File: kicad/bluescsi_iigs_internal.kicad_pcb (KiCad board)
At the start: 2 copper layers, 61.5 x 55.4 mm, 27 parts, among them J1 Conn_02x13_Odd_Even, J2 Conn_02x13_Odd_Even, J3 105162-0001, J4 Conn_01x02_Male, J5 Conn_01x02_Male, J6 DB25_Male, M1 Screw_Terminal_01x01, M2 Screw_Terminal_01x01, SW1 SW_SPDT, U1 YAAJ_BluePill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

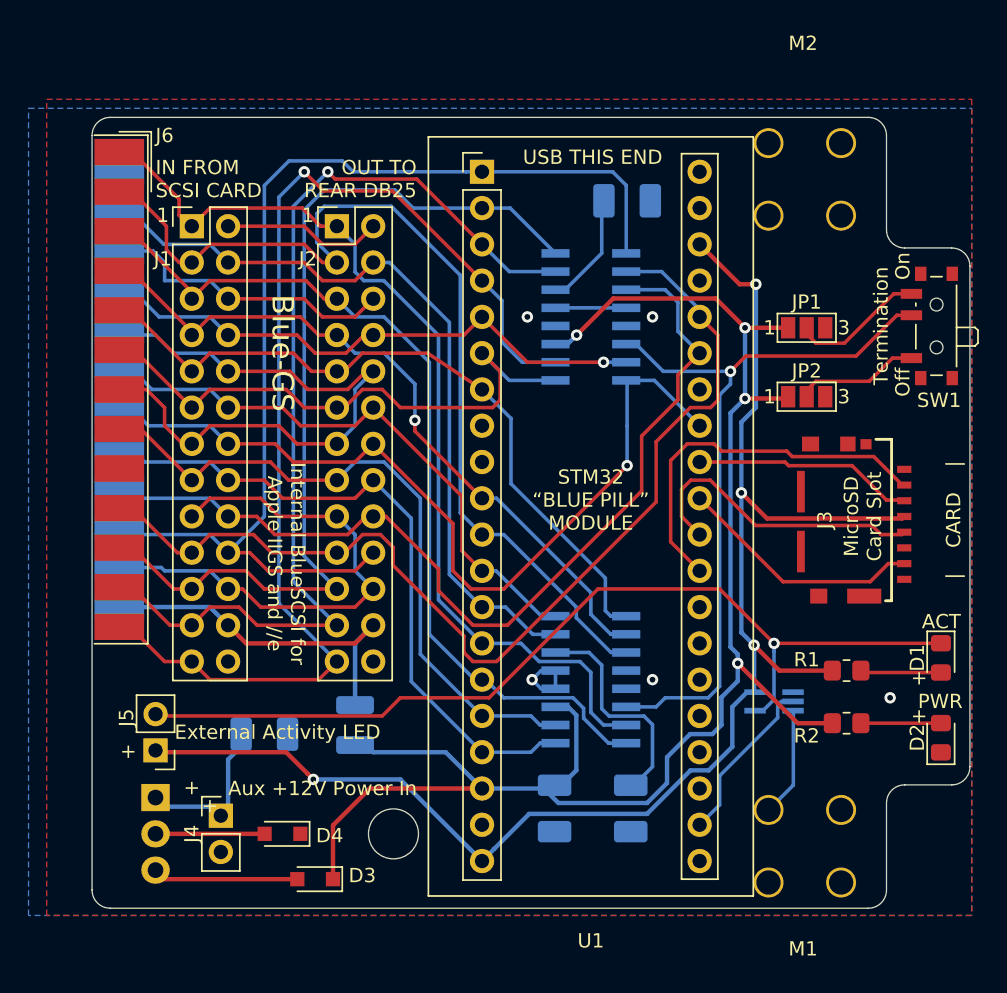
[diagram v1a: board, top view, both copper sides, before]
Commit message: Change silkscreens and legends, reroute 3.3v line for better grounding
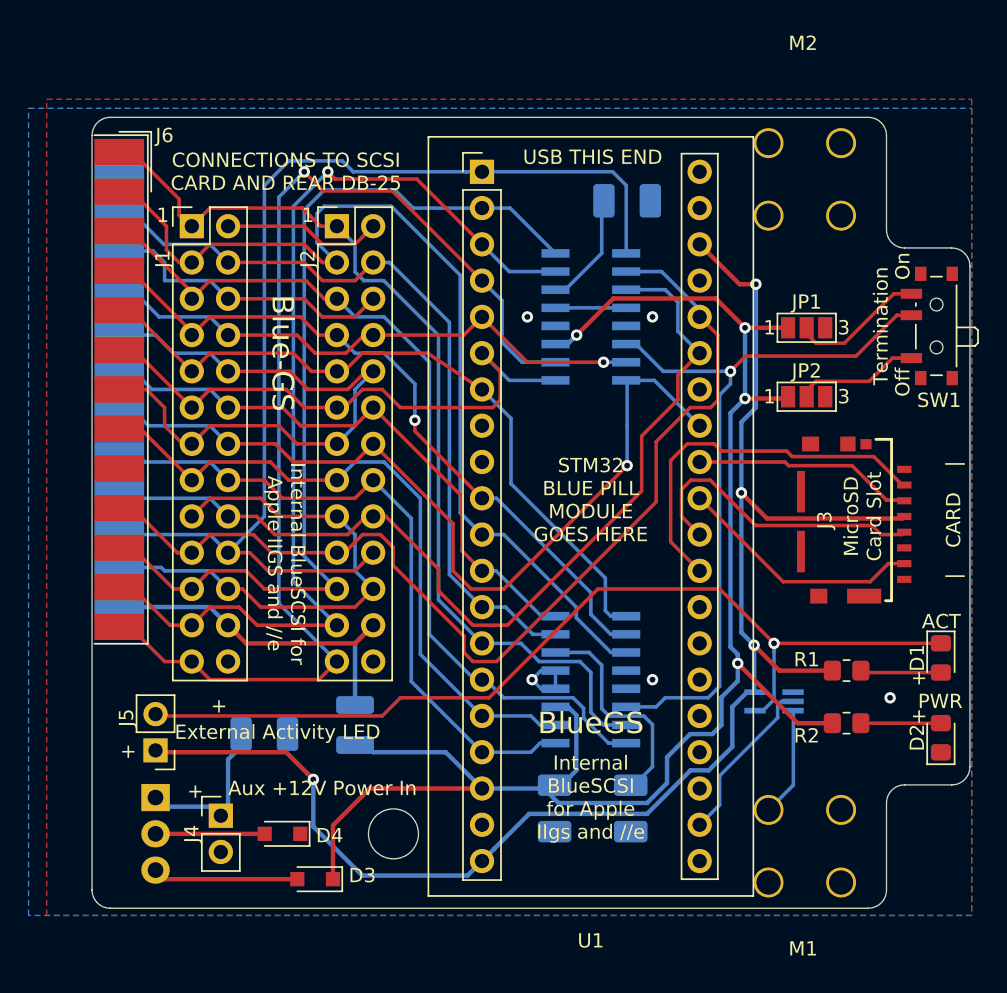
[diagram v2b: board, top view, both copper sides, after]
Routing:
- net +3V3: track 104.0 -> 106.8 mm
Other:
- board text added: "BlueGS"
- board text added: "CONNECTIONS TO SCSI CARD AND REAR DB-25"
- board text added: "Internal BlueSCSI for Apple IIgs and //e"
- board text added: "STM32 BLUE PILL MODULE GOES HERE"
- board text removed: "For Apple Rev. C SCSI and cards with compatible connector"
- board text removed: "IN FROM SCSI CARD"
- board text removed: "OUT TO REAR DB25"
- board text removed: "STM32 “BLUE PILL” MODULE"
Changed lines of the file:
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@@
     (thickness 1.6)
     (drawings 59)
-    (tracks 579)
+    (tracks 581)
     (zones 0)
     (modules 27)
@@
     (descr "Through hole straight pin header, 2x13, 2.54mm pitch, double rows")
     (tags "Through hole pin header THT 2x13 2.54mm double row")
-    (fp_text reference J2 (at -2.032 2.286) (layer F.SilkS)
+    (fp_text reference J2 (at -2.032 2.286 90) (layer F.SilkS)
       (effects (font (size 1 1) (thickness 0.15)))
     )
@@
     (descr "Through hole straight pin header, 2x13, 2.54mm pitch, double rows")
     (tags "Through hole pin header THT 2x13 2.54mm double row")
-    (fp_text reference J1 (at -2.032 2.286) (layer F.SilkS)
+    (fp_text reference J1 (at -2.032 2.286 90) (layer F.SilkS)
       (effects (font (size 1 1) (thickness 0.15)))
     )
@@
     )
   )
+  (gr_text "Internal\nBlueSCSI\nfor Apple\nIIgs and //e" (at 160.02 94.615) (layer F.SilkS)
+    (effects (font (size 1 1) (thickness 0.15)))
+  )
+  (gr_text BlueGS (at 160.02 89.408) (layer F.SilkS)
+    (effects (font (size 1.5 1.5) (thickness 0.2)))
+  )
   (gr_text "|    CARD    |" (at 185.42 75.184 90) (layer F.SilkS)
     (effects (font (size 1 1) (thickness 0.15)))
@@
     (effects (font (size 1.5 1.5) (thickness 0.15)))
   )
-  (gr_text "v1.3 (6/2021)" (at 179.07 67.31 90) (layer B.SilkS)
+  (gr_text "v1.3 (6/2021)" (at 177.8 84.836 90) (layer B.SilkS)
     (effects (font (size 1 1) (thickness 0.15)) (justify mirror))
   )
-  (gr_text Blue-GS (at 171.45 67.31 90) (layer B.SilkS)
-    (effects (font (size 1.5 1.5) (thickness 0.15)) (justify mirror))
-  )
-  (gr_text + (at 133.35 95.25 180) (layer F.SilkS)
+  (gr_text Blue-GS (at 173.736 67.31 90) (layer B.SilkS)
+    (effects (font (size 1.5 1.5) (thickness 0.2)) (justify mirror))
+  )
+  (gr_text + (at 133.985 88.265 180) (layer F.SilkS)
     (effects (font (size 1 1) (thickness 0.15)))
   )
-  (gr_text + (at 132.08 93.98 180) (layer F.SilkS)
+  (gr_text + (at 132.334 94.234 180) (layer F.SilkS)
     (effects (font (size 1 1) (thickness 0.15)))
   )
@@
     (effects (font (size 1 1) (thickness 0.15)) (justify left))
   )
-  (gr_text "Internal BlueSCSI for\nApple IIGS and //e" (at 175.26 67.056 90) (layer B.SilkS)
+  (gr_text "Internal BlueSCSI for\nApple IIGS and //e" (at 177.8 67.056 90) (layer B.SilkS)
     (effects (font (size 1 1) (thickness 0.15)) (justify mirror))
   )
@@
     (arrow2b (pts (xy 190.5 56.134) (xy 191.086421 57.260504)))
   )
-  (gr_text "For Apple Rev. C SCSI\nand cards with\ncompatible connector" (at 177.8 83.058 90) (layer B.SilkS)
-    (effects (font (size 0.75 0.75) (thickness 0.1)) (justify mirror))
-  )
   (gr_text "MicroSD\nCard Slot" (at 179.07 74.93 90) (layer F.SilkS)
     (effects (font (size 1 1) (thickness 0.15)))
@@
     (effects (font (size 1 1) (thickness 0.15)) (justify right))
   )
-  (gr_text github.com/xunker/blue-gs (at 138.684 75.184 90) (layer B.SilkS)
+  (gr_text github.com/xunker/blue-gs (at 138.684 69.596 90) (layer B.SilkS)
     (effects (font (size 1 1) (thickness 0.15)) (justify mirror))
   )
@@
     (effects (font (size 1 1) (thickness 0.15)) (justify mirror))
   )
-  (gr_text "STM32\n“BLUE PILL”\nMODULE" (at 160.02 73.787) (layer F.SilkS)
+  (gr_text "STM32\nBLUE PILL\nMODULE\nGOES HERE" (at 160.02 73.787) (layer F.SilkS)
     (effects (font (size 1 1) (thickness 0.15)))
   )
@@
     (effects (font (size 1 1) (thickness 0.15)))
   )
-  (gr_text "OUT TO\nREAR DB25\n" (at 147.828 51.308) (layer F.SilkS)
-    (effects (font (size 1 1) (thickness 0.15)) (justify right))
-  )
-  (gr_text "IN FROM\nSCSI CARD" (at 129.54 51.308) (layer F.SilkS)
-    (effects (font (size 1 1) (thickness 0.15)) (justify left))
+  (gr_text "CONNECTIONS TO SCSI\nCARD AND REAR DB-25" (at 138.684 50.8) (layer F.SilkS)
+    (effects (font (size 1 1) (thickness 0.15)))
   )
   (dimension 55.372 (width 0.15) (layer Dwgs.User)
@@
   (segment (start 181.823001 75.075999) (end 172.357999 75.075999) (width 0.31) (layer F.Cu) (net 34))
   (segment (start 181.965 74.934) (end 181.823001 75.075999) (width 0.31) (layer F.Cu) (net 34))
-  (segment (start 152.4 99.06) (end 146.685 93.345) (width 0.31) (layer B.Cu) (net 34))
-  (segment (start 146.685 93.345) (end 140.589 93.345) (width 0.31) (layer B.Cu) (net 34))
   (via (at 140.589 93.345) (size 0.8) (drill 0.4) (layers F.Cu B.Cu) (net 34))
   (segment (start 138.684 91.44) (end 140.189001 92.945001) (width 0.31) (layer F.Cu) (net 34))
@@
   (segment (start 140.189001 92.945001) (end 140.589 93.345) (width 0.31) (layer F.Cu) (net 34))
   (segment (start 129.54 91.313) (end 129.667 91.44) (width 0.31) (layer F.Cu) (net 34))
+  (segment (start 140.589 96.647) (end 140.589 93.345) (width 0.31) (layer B.Cu) (net 34))
+  (segment (start 144.018 100.076) (end 140.589 96.647) (width 0.31) (layer B.Cu) (net 34))
+  (segment (start 151.384 100.076) (end 144.018 100.076) (width 0.31) (layer B.Cu) (net 34))
+  (segment (start 152.4 99.06) (end 151.384 100.076) (width 0.31) (layer B.Cu) (net 34))
   (segment (start 181.918 73.787) (end 181.965 73.834) (width 0.25) (layer F.Cu) (net 35))
   (segment (start 180.721 73.787) (end 181.918 73.787) (width 0.25) (layer F.Cu) (net 35))

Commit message: move some vias for better ground fill
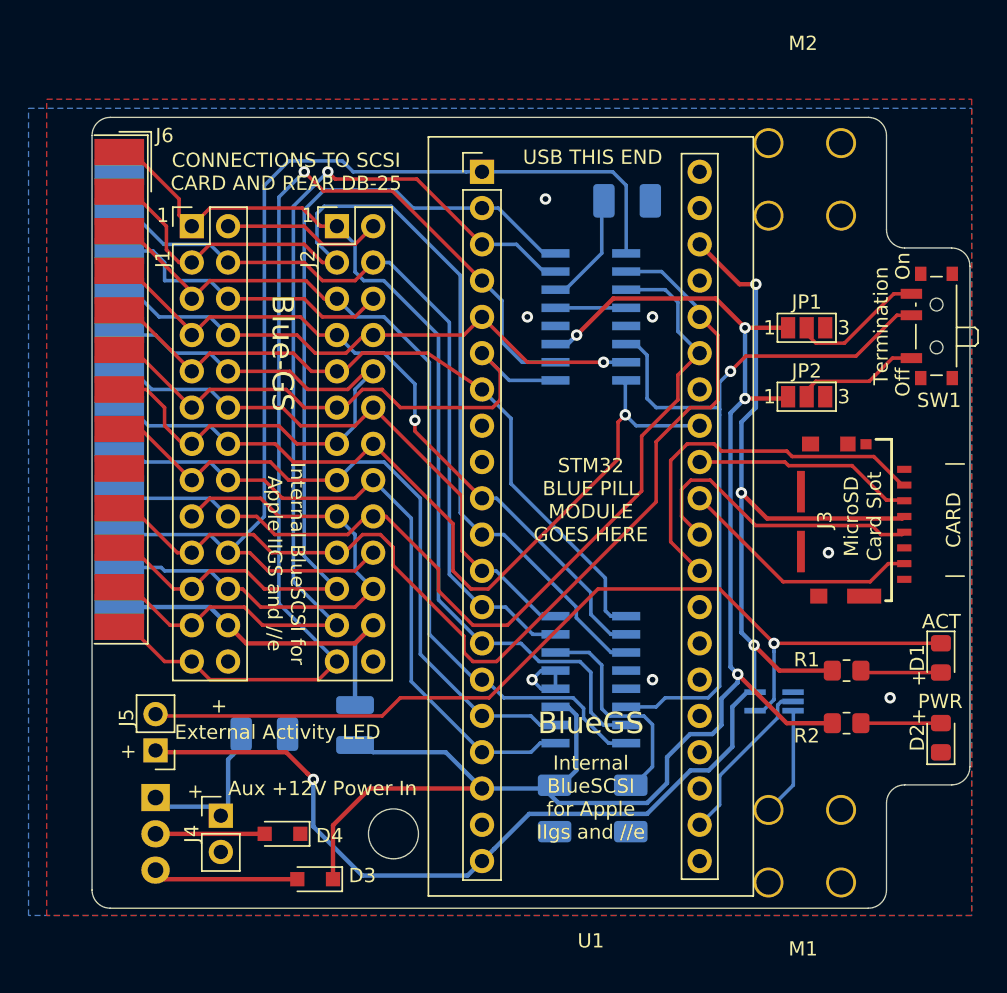
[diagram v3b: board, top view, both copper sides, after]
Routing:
- net /TERM_DISC: track 52.1 -> 54.3 mm
- net /SCSI_DBP: track 59.8 -> 58.2 mm
- net GND: vias 5 -> 7

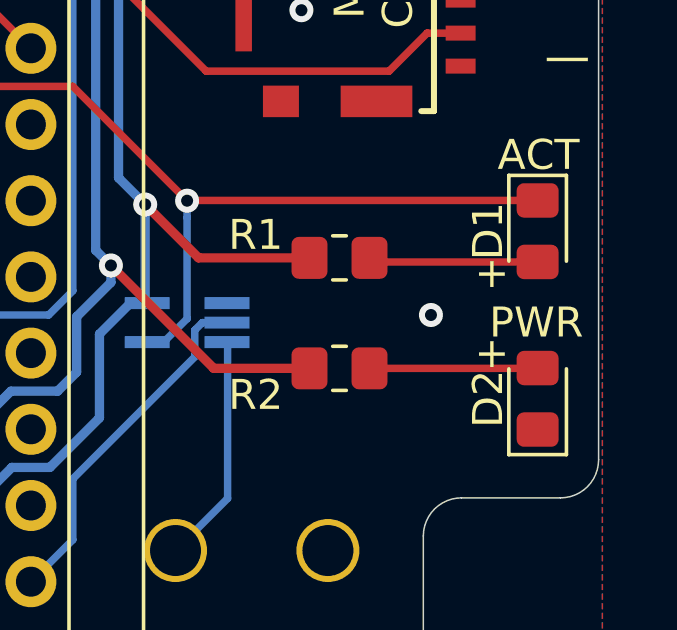
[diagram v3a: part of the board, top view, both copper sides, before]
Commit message: Re-annotate schematic for connectors add SN field
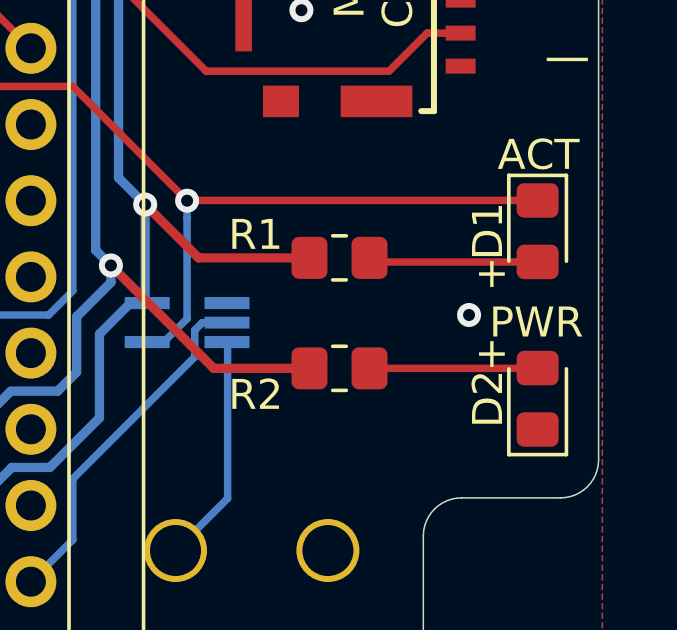
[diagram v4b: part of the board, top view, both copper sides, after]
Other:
- board text added: "SN #"
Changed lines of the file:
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@@
   (general
     (thickness 1.6)
-    (drawings 59)
+    (drawings 61)
     (tracks 588)
     (zones 0)
@@
     )
   )
+  (gr_poly (pts (xy 180.34 89.535) (xy 177.165 89.535) (xy 177.165 84.455) (xy 180.34 84.455)) (layer B.SilkS) (width 0.1))
+  (gr_text "SN #" (at 178.435 81.915 90) (layer B.SilkS)
+    (effects (font (size 1 1) (thickness 0.15)) (justify mirror))
+  )
   (gr_text "Internal\nBlueSCSI\nfor Apple\nIIgs and //e" (at 160.02 94.615) (layer F.SilkS)
     (effects (font (size 1 1) (thickness 0.15)))
@@
     (effects (font (size 1.5 1.5) (thickness 0.15)))
   )
-  (gr_text "v1.3 (6/2021)" (at 177.8 84.836 90) (layer B.SilkS)
+  (gr_text "v1.3 (6/2021)" (at 175.895 84.836 90) (layer B.SilkS)
     (effects (font (size 1 1) (thickness 0.15)) (justify mirror))
   )
@@
   (segment (start 157.545 86.995) (end 156.5402 86.995) (width 0.25) (layer B.Cu) (net 13))
   (via (at 155.9052 86.36) (size 0.8) (drill 0.4) (layers F.Cu B.Cu) (net 13))
-  (via (at 180.975 87.63) (size 0.8) (drill 0.4) (layers F.Cu B.Cu) (net 13))
+  (via (at 182.245 87.63) (size 0.8) (drill 0.4) (layers F.Cu B.Cu) (net 13))
   (segment (start 174.197 93.745) (end 172.461 95.481) (width 0.25) (layer B.Cu) (net 13))
   (segment (start 174.197 88.58) (end 174.197 93.745) (width 0.25) (layer B.Cu) (net 13))

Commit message: v1.3.1 commit
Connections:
- J1 pad 26: Net-(J1-Pad26) -> unconnected-(J1-Pad26)
- J2 pad 26: Net-(J2-Pad26) -> unconnected-(J2-Pad26)
- J3 pad 1: Net-(J3-Pad1) -> unconnected-(J3-Pad1)
- J3 pad 8: Net-(J3-Pad8) -> unconnected-(J3-Pad8)
- U1 pad 21: Net-(U1-Pad21) -> unconnected-(U1-Pad21)
- U1 pad 23: Net-(U1-Pad23) -> unconnected-(U1-Pad23)
- U1 pad 24: Net-(U1-Pad24) -> unconnected-(U1-Pad24)
- U1 pad 25: Net-(U1-Pad25) -> unconnected-(U1-Pad25)
- U1 pad 28: Net-(U1-Pad28) -> unconnected-(U1-Pad28)
- U1 pad 34: Net-(U1-Pad34) -> unconnected-(U1-Pad34)
- U1 pad 37: Net-(U1-Pad37) -> unconnected-(U1-Pad37)
- U1 pad 8: Net-(U1-Pad8) -> unconnected-(U1-Pad8)
- U1 pad 9: Net-(U1-Pad9) -> unconnected-(U1-Pad9)
- U5 pad 1: Net-(U5-Pad1) -> unconnected-(U5-Pad1)
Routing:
- net /SCSI_ACK: track 51.6 -> 50.2 mm
- net /SCSI_SEL: track 42.0 -> 41.0 mm
- net /SCSI_DB0: track 48.5 -> 47.6 mm
- net /SCSI_ATN: track 40.2 -> 39.7 mm
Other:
- net class Default removed
- net class POWER removed
- board text added: "CC BY-SA-NC/4.0"
- board text added: "v1.3.1 (4/2022)"
- board text removed: "v1.3 (6/2021)"

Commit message: I should have done a changelog a long time ago
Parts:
- D3, D4: value 1N4001 -> 1N5319; footprint Diode_SMD:D_SOD-323_HandSoldering -> Diode_SMD:D_SOD-123
- R1: value 470 -> 110
- moved J5 1.65 mm to (127.9, 91.3)
- moved D4 1.27 mm to (139.7, 97.2)
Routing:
- net GND: track 131.6 -> 134.2 mm, vias 7 -> 6
- net +3V3: track 106.8 -> 108.9 mm
- net /SD_MISO: track 17.3 -> 16.2 mm
- net +5V: track 112.9 -> 112.0 mm
- net Net-(D4-Pad2): track 7.64 -> 8.51 mm
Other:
- board text added: "v1.3.2 (10/2022)"
- board text removed: "v1.3.1 (4/2022)"

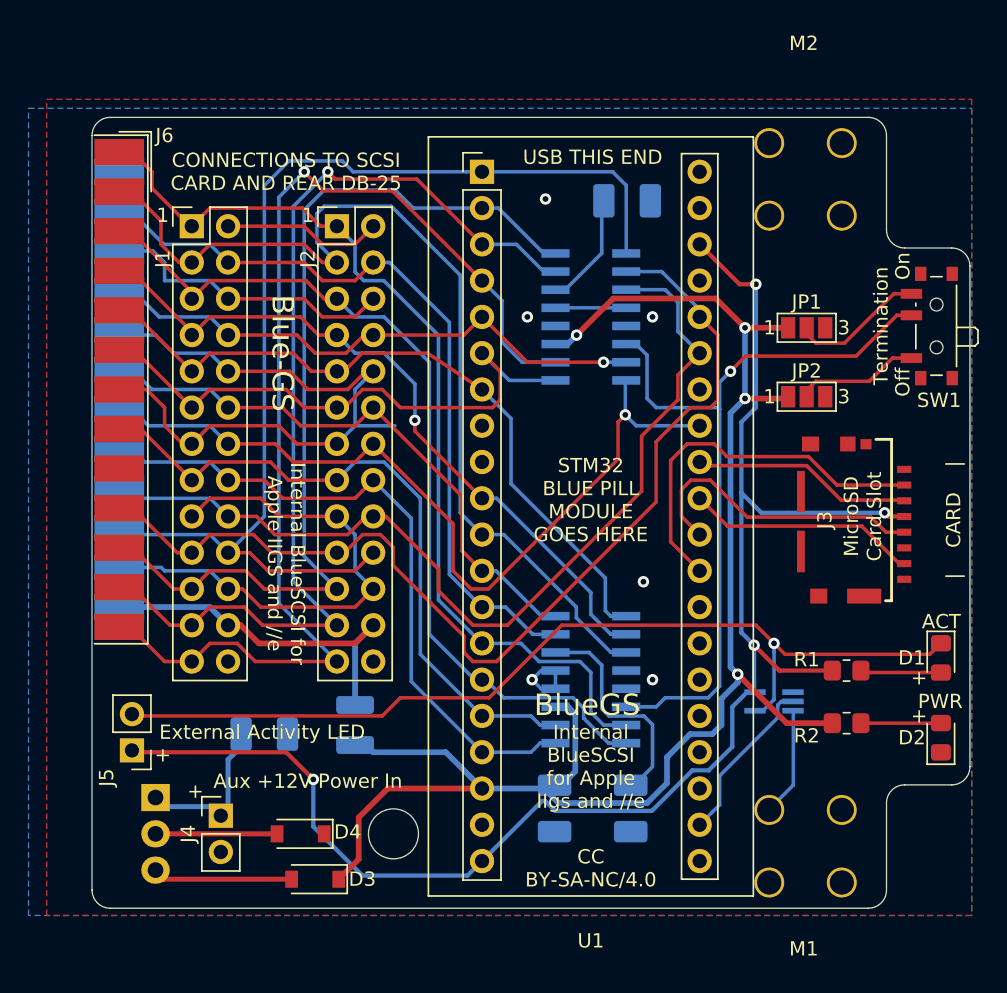
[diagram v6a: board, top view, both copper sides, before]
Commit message: Change 7805 to UCC3916; nudge some traces to get better gnds
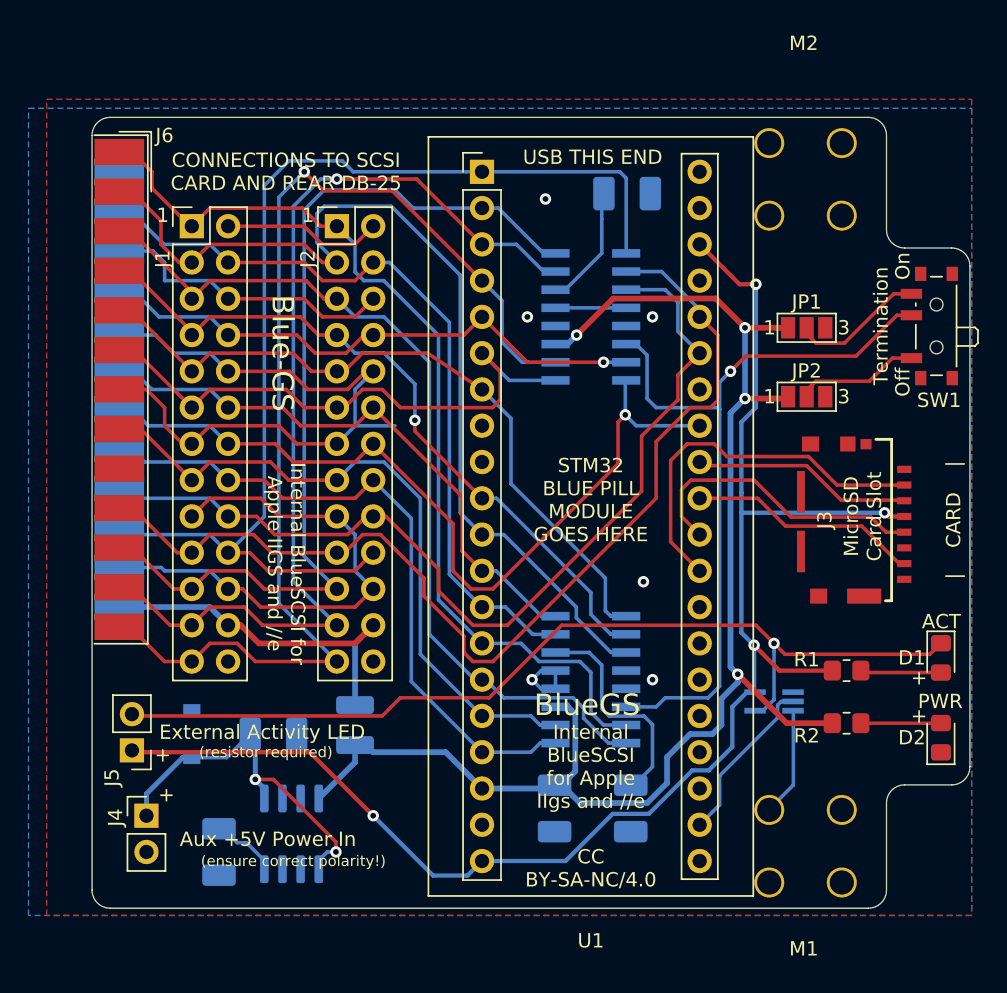
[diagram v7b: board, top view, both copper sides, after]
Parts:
- removed D4: 1N5319, Diode_SMD:D_SOD-123
- added C5: 0.1uF, Capacitor_Tantalum_SMD:CP_EIA-3528-21_Kemet-B_Pad1.50x2.35mm_HandSolder, B.Cu at (134.0, 98.4)
- C4: value 10uF -> 1uF
- D3: value 1N5319 -> Zener 5.6v; moved to B.Cu
- U4: value MC7805CT-BP -> UCC3916; footprint Package_TO_SOT_THT:TO-220-3_Horizontal_TabUp -> Package_SO:SOIC-8_3.9x4.9mm_P1.27mm
- moved D3 13.3 mm to (132.1, 90.2), turned to 90 degrees
- moved U4 9.86 mm to (139.1, 97.2), turned to 90 degrees
- moved J4 5.21 mm to (128.9, 95.9)
- moved C4 0.63 mm to (137.8, 90.2)
- moved C1 0.51 mm to (162.6, 52.3)
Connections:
- C4 pad 1: /+12V_AUX -> /+5V_AUX
- D3 pad 1: +5V -> /+5V_AUX
- D3 pad 2: /REG_OUT -> GND
- J4 pad 1: /+12V_AUX -> /+5V_AUX
- U4 pad 1: /+12V_AUX -> /+5V_AUX
- U4 pad 2: Net-(D4-Pad2) -> GND
- U4 pad 3: /REG_OUT -> GND
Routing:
- net /+5V_AUX: track 0.00 -> 25.7 mm, vias 0 -> 2
- net /+12V_AUX: track 10.5 -> 0.00 mm
- net +5V: track 112.0 -> 101.7 mm
- net /REG_OUT: track 9.79 -> 0.00 mm
- net Net-(D4-Pad2): track 8.51 -> 0.00 mm
- net Net-(C5-Pad1): track 0.00 -> 4.70 mm
- net +3V3: track 108.9 -> 105.8 mm
- net Net-(C1-Pad1): track 7.63 -> 8.54 mm
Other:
- board text added: "(ensure correct polarity!)"
- board text added: "(resistor required)"
- board text added: "Aux +5V Power In"
- board text added: "v1.4 (11/2022)"
- board text removed: "Aux +12V Power In"
- board text removed: "SN #"
- board text removed: "v1.3.2 (10/2022)"
